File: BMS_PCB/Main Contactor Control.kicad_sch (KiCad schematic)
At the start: 1 part, among them U10 ULN2003A

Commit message: Footprints changes
-U10
-uC pins/SPI changes
- Fuses
- DSUB
- reupload layout
- etc.
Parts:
- U10: footprint Package_TO_SOT_SMD:SOT-23-6_Handsoldering -> Package_SO:SOIC-16_3.9x9.9mm_P1.27mm
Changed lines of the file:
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@@
 			)
 		)
-		(property "Footprint" "Package_TO_SOT_SMD:SOT-23-6_Handsoldering"
+		(property "Footprint" "Package_SO:SOIC-16_3.9x9.9mm_P1.27mm"
 			(at 92.71 66.04 0)
 			(effects

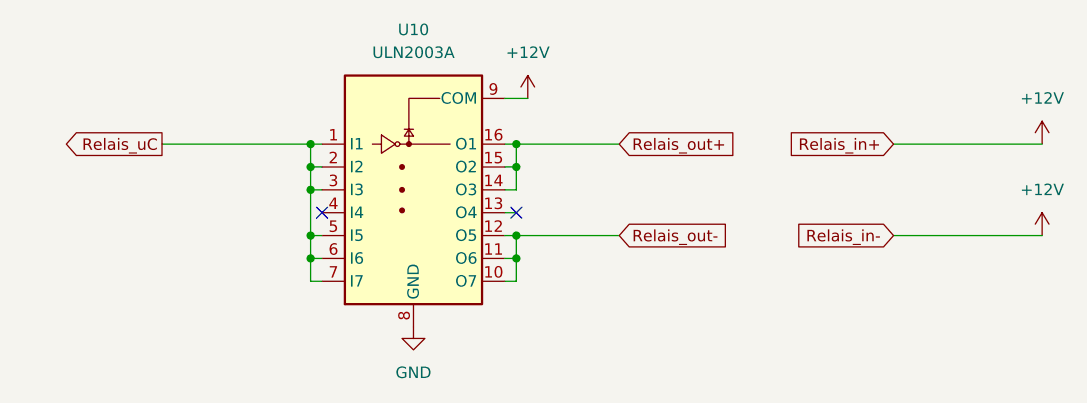
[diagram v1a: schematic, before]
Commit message: changes schematic
still missing: uC pins
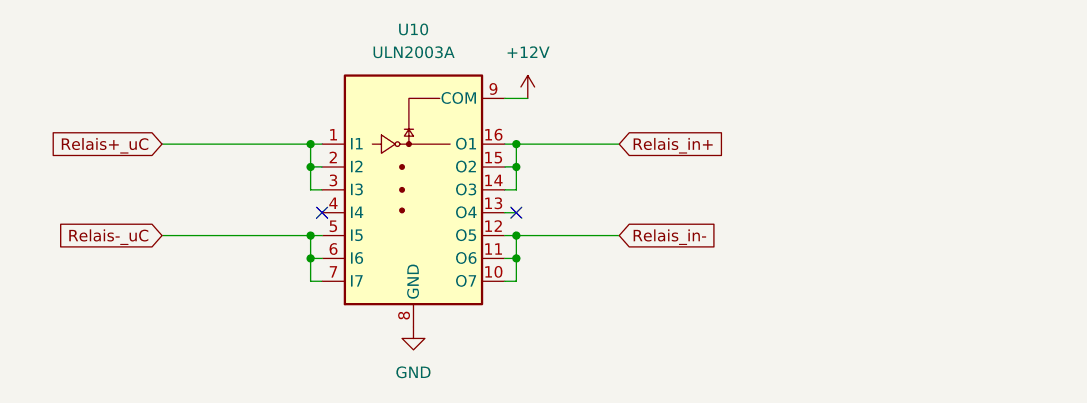
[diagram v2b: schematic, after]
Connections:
- net Relais_out+ renamed Relais_in+
- net Relais_out- renamed Relais_in-
- net Relais_uC renamed Relais+_uC
- net Relais+_uC: no longer U10.5 (I5), U10.6 (I6), U10.7 (I7)
- new net Relais-_uC: U10.5 (I5), U10.6 (I6), U10.7 (I7)
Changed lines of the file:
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@@
 	)
 	(junction
-		(at 80.01 52.07)
+		(at 80.01 57.15)
 		(diameter 0)
 		(color 0 0 0 0)
@@
 	(junction
 		(at 102.87 46.99)
-		(diameter 0)
-		(color 0 0 0 0)
-	)
-	(junction
-		(at 80.01 57.15)
 		(diameter 0)
 		(color 0 0 0 0)
@@
 	(wire
 		(pts
+			(xy 63.5 57.15) (xy 80.01 57.15)
+		)
+		(stroke
+			(width 0)
+			(type default)
+		)
+	)
+	(wire
+		(pts
 			(xy 102.87 57.15) (xy 102.87 59.69)
 		)
@@
 	(wire
 		(pts
-			(xy 144.78 46.99) (xy 161.29 46.99)
-		)
-		(stroke
-			(width 0)
-			(type default)
-		)
-	)
-	(wire
-		(pts
 			(xy 102.87 46.99) (xy 102.87 49.53)
 		)
@@
 	(wire
 		(pts
-			(xy 80.01 52.07) (xy 80.01 57.15)
-		)
-		(stroke
-			(width 0)
-			(type default)
-		)
-	)
-	(wire
-		(pts
-			(xy 144.78 57.15) (xy 161.29 57.15)
-		)
-		(stroke
-			(width 0)
-			(type default)
-		)
-	)
-	(wire
-		(pts
 			(xy 102.87 57.15) (xy 114.3 57.15)
 		)
@@
 		)
 	)
-	(global_label "Relais_uC"
-		(shape output)
+	(global_label "Relais+_uC"
+		(shape input)
 		(at 63.5 46.99 180)
 		(fields_autoplaced yes)
@@
 		)
 		(property "Intersheetrefs" "${INTERSHEET_REFS}"
-			(at 51.3225 46.99 0)
+			(at 49.7501 46.99 0)
 			(effects
 				(font
@@
 		)
 	)
-	(global_label "Relais_out+"
+	(global_label "Relais_in+"
 		(shape input)
 		(at 114.3 46.99 0)
@@
 		)
 		(property "Intersheetrefs" "${INTERSHEET_REFS}"
-			(at 128.6546 46.99 0)
+			(at 127.3847 46.99 0)
 			(effects
 				(font
@@
 		)
 	)
-	(global_label "Relais_in+"
-		(shape input)
-		(at 144.78 46.99 180)
-		(fields_autoplaced yes)
-		(effects
-			(font
-				(size 1.27 1.27)
-			)
-			(justify right)
-		)
-		(property "Intersheetrefs" "${INTERSHEET_REFS}"
-			(at 131.6953 46.99 0)
-			(effects
-				(font
-					(size 1.27 1.27)
-				)
-				(justify right)
-				(hide yes)
-			)
-		)
-	)
-	(global_label "Relais_out-"
+	(global_label "Relais_in-"
 		(shape input)
 		(at 114.3 57.15 0)
@@
 		)
 		(property "Intersheetrefs" "${INTERSHEET_REFS}"
-			(at 128.6546 57.15 0)
+			(at 127.3847 57.15 0)
 			(effects
 				(font
@@
 		)
 	)
-	(global_label "Relais_in-"
+	(global_label "Relais-_uC"
 		(shape input)
-		(at 144.78 57.15 180)
+		(at 63.5 57.15 180)
 		(fields_autoplaced yes)
 		(effects
@@
 		)
 		(property "Intersheetrefs" "${INTERSHEET_REFS}"
-			(at 131.6953 57.15 0)
+			(at 49.7501 57.15 0)
 			(effects
 				(font
@@
 					(unit 1)
 				)
-			)
-		)
-	)
-	(symbol
-		(lib_id "power:+12V")
-		(at 161.29 57.15 0)
-		(unit 1)
-		(exclude_from_sim no)
-		(in_bom yes)
-		(on_board yes)
-		(dnp no)
-		(fields_autoplaced yes)
-		(property "Reference" "#PWR0114"
-			(at 161.29 60.96 0)
-			(effects
-				(font
-					(size 1.27 1.27)
-				)
-				(hide yes)
-			)
-		)
-		(property "Value" "+12V"
-			(at 161.29 52.07 0)
-			(effects
-				(font
-					(size 1.27 1.27)
-				)
-			)
-		)
-		(property "Footprint" ""
-			(at 161.29 57.15 0)
-			(effects
-				(font
-					(size 1.27 1.27)
-				)
-				(hide yes)
-			)
-		)
-		(property "Datasheet" ""
-			(at 161.29 57.15 0)
-			(effects
-				(font
-					(size 1.27 1.27)
-				)
-				(hide yes)
-			)
-		)
-		(property "Description" "Power symbol creates a global label with name \"+12V\""
-			(at 161.29 57.15 0)
-			(effects
-				(font
-					(size 1.27 1.27)
-				)
-				(hide yes)
-			)
-		)
-		(pin "1"
-		)
-		(instances
-			(project ""
-				(path "/f3f5bf67-59a2-4fff-a256-b414fb7b1786/70268bf0-6659-4886-b5bd-e8e42422f194"
-					(reference "#PWR0114")
-					(unit 1)
-				)
-			)
-		)
-	)
-	(symbol
-		(lib_id "power:+12V")
-		(at 161.29 46.99 0)
-		(unit 1)
-		(exclude_from_sim no)
-		(in_bom yes)
-		(on_board yes)
-		(dnp no)
-		(fields_autoplaced yes)
-		(property "Reference" "#PWR0112"
-			(at 161.29 50.8 0)
-			(effects
-				(font
-					(size 1.27 1.27)
-				)
-				(hide yes)
-			)
-		)
-		(property "Value" "+12V"
-			(at 161.29 41.91 0)
-			(effects
-				(font
-					(size 1.27 1.27)
-				)
-			)
-		)
-		(property "Footprint" ""
-			(at 161.29 46.99 0)
-			(effects
-				(font
-					(size 1.27 1.27)
-				)
-				(hide yes)
-			)
-		)
-		(property "Datasheet" ""
-			(at 161.29 46.99 0)
-			(effects
-				(font
-					(size 1.27 1.27)
-				)
-				(hide yes)
-			)
-		)
-		(property "Description" "Power symbol creates a global label with name \"+12V\""
-			(at 161.29 46.99 0)
-			(effects
-				(font
-					(size 1.27 1.27)
-				)
-				(hide yes)
-			)
-		)
-		(pin "1"
-		)
-		(instances
-			(project ""
-				(path "/f3f5bf67-59a2-4fff-a256-b414fb7b1786/70268bf0-6659-4886-b5bd-e8e42422f194"
-					(reference "#PWR0112")
-					(unit 1)
-				)
